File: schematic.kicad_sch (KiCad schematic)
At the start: 6 parts, among them J1 Controller, U1 ATtiny85

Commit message: pulldown
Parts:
- added R1: 100k, symbol Device:R_US
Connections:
- net Earth: now also R1.2
- net at RV1.2, U1.7 (PB2): now also R1.1
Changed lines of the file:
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@@
   (junction (at 175.26 83.82) (diameter 0) (color 0 0 0 0)
   )
-  (junction (at 149.86 115.57) (diameter 0) (color 0 0 0 0)
+  (junction (at 149.86 115.57) (diameter 0) (color 0 0 0 1)
   )
   (junction (at 166.37 115.57) (diameter 0) (color 0 0 0 1)
   )
-  (junction (at 121.92 64.77) (diameter 0) (color 194 0 0 1)
-  )
-  (junction (at 186.69 115.57) (diameter 0) (color 0 0 0 0)
-  )
-  (junction (at 166.37 64.77) (diameter 0) (color 194 0 0 1)
-  )
-  (junction (at 149.86 64.77) (diameter 0) (color 194 0 0 1)
-  )
-  (junction (at 137.16 64.77) (diameter 0) (color 194 0 0 1)
+  (junction (at 121.92 69.85) (diameter 0) (color 194 0 0 1)
+  )
+  (junction (at 186.69 115.57) (diameter 0) (color 0 0 0 1)
+  )
+  (junction (at 166.37 69.85) (diameter 0) (color 194 0 0 1)
+  )
+  (junction (at 149.86 69.85) (diameter 0) (color 194 0 0 1)
+  )
+  (junction (at 137.16 69.85) (diameter 0) (color 194 0 0 1)
+  )
+  (junction (at 139.7 115.57) (diameter 0) (color 0 0 0 1)
   )
   (junction (at 121.92 115.57) (diameter 0) (color 0 0 0 1)
   )
+  (junction (at 139.7 105.41) (diameter 0) (color 0 0 0 0)
+  )
   (junction (at 175.26 115.57) (diameter 0) (color 0 0 0 1)
   )
+  (wire (pts (xy 139.7 115.57) (xy 149.86 115.57))
+    (stroke (width 0) (type default) (color 0 0 0 1))
+  )
   (wire (pts (xy 158.75 96.52) (xy 158.75 88.9))
     (stroke (width 0) (type default))
@@
     (stroke (width 0) (type default))
   )
-  (wire (pts (xy 121.92 115.57) (xy 149.86 115.57))
-    (stroke (width 0) (type default) (color 0 0 0 1))
-  )
-  (wire (pts (xy 101.6 106.68) (xy 101.6 96.52))
+  (wire (pts (xy 121.92 115.57) (xy 139.7 115.57))
+    (stroke (width 0) (type default) (color 0 0 0 1))
+  )
+  (wire (pts (xy 101.6 105.41) (xy 101.6 96.52))
     (stroke (width 0) (type default))
   )
@@
     (stroke (width 0) (type default) (color 0 0 0 1))
   )
-  (wire (pts (xy 166.37 64.77) (xy 166.37 92.71))
-    (stroke (width 0) (type default) (color 194 0 0 1))
-  )
-  (wire (pts (xy 149.86 93.98) (xy 149.86 64.77))
+  (wire (pts (xy 166.37 69.85) (xy 166.37 92.71))
+    (stroke (width 0) (type default) (color 194 0 0 1))
+  )
+  (wire (pts (xy 149.86 93.98) (xy 149.86 69.85))
     (stroke (width 0) (type default) (color 194 0 0 1))
   )
@@
     (stroke (width 0) (type default) (color 0 0 0 1))
   )
-  (wire (pts (xy 96.52 92.71) (xy 96.52 64.77))
+  (wire (pts (xy 96.52 92.71) (xy 96.52 69.85))
     (stroke (width 0) (type default) (color 194 0 0 1))
   )
@@
   )
   (wire (pts (xy 186.69 118.11) (xy 186.69 115.57))
-    (stroke (width 0) (type default))
-  )
-  (wire (pts (xy 137.16 64.77) (xy 149.86 64.77))
+    (stroke (width 0) (type default) (color 0 0 0 1))
+  )
+  (wire (pts (xy 137.16 69.85) (xy 149.86 69.85))
     (stroke (width 0) (type default) (color 194 0 0 1))
   )
@@
     (stroke (width 0) (type default) (color 0 0 0 1))
   )
-  (wire (pts (xy 121.92 64.77) (xy 121.92 73.66))
-    (stroke (width 0) (type default) (color 194 0 0 1))
-  )
-  (wire (pts (xy 149.86 64.77) (xy 166.37 64.77))
+  (wire (pts (xy 121.92 69.85) (xy 121.92 73.66))
+    (stroke (width 0) (type default) (color 194 0 0 1))
+  )
+  (wire (pts (xy 149.86 69.85) (xy 166.37 69.85))
     (stroke (width 0) (type default) (color 194 0 0 1))
   )
@@
     (stroke (width 0) (type default) (color 0 0 0 1))
   )
-  (wire (pts (xy 186.69 81.28) (xy 186.69 64.77))
+  (wire (pts (xy 186.69 81.28) (xy 186.69 69.85))
     (stroke (width 0) (type default) (color 194 0 0 1))
   )
@@
     (stroke (width 0) (type default) (color 0 132 0 1))
   )
-  (wire (pts (xy 139.7 86.36) (xy 139.7 106.68))
+  (wire (pts (xy 139.7 86.36) (xy 139.7 105.41))
+    (stroke (width 0) (type default))
+  )
+  (wire (pts (xy 139.7 105.41) (xy 139.7 106.68))
     (stroke (width 0) (type default))
   )
@@
     (stroke (width 0) (type default) (color 0 132 0 1))
   )
-  (wire (pts (xy 139.7 106.68) (xy 101.6 106.68))
-    (stroke (width 0) (type default))
-  )
-  (wire (pts (xy 166.37 64.77) (xy 186.69 64.77))
-    (stroke (width 0) (type default) (color 194 0 0 1))
-  )
-  (wire (pts (xy 121.92 64.77) (xy 137.16 64.77))
+  (wire (pts (xy 139.7 105.41) (xy 101.6 105.41))
+    (stroke (width 0) (type default))
+  )
+  (wire (pts (xy 166.37 69.85) (xy 186.69 69.85))
+    (stroke (width 0) (type default) (color 194 0 0 1))
+  )
+  (wire (pts (xy 121.92 69.85) (xy 137.16 69.85))
     (stroke (width 0) (type default) (color 194 0 0 1))
   )
@@
     (stroke (width 0) (type default) (color 0 0 0 1))
   )
-  (wire (pts (xy 96.52 64.77) (xy 121.92 64.77))
+  (wire (pts (xy 96.52 69.85) (xy 121.92 69.85))
     (stroke (width 0) (type default) (color 194 0 0 1))
   )
@@
     (stroke (width 0) (type default))
   )
-  (wire (pts (xy 137.16 64.77) (xy 137.16 81.28))
+  (wire (pts (xy 137.16 69.85) (xy 137.16 81.28))
     (stroke (width 0) (type default) (color 194 0 0 1))
   )
@@
     (stroke (width 0) (type default) (color 0 0 0 1))
   )
+  (wire (pts (xy 139.7 114.3) (xy 139.7 115.57))
+    (stroke (width 0) (type default) (color 0 0 0 1))
+  )
   (wire (pts (xy 101.6 96.52) (xy 100.33 96.52))
-    (stroke (width 0) (type default))
-  )
-  (wire (pts (xy 186.69 115.57) (xy 181.61 115.57))
     (stroke (width 0) (type default))
   )
@@
         )
       )
+    )
+  )
+  (symbol (lib_id "Device:R_US") (at 139.7 110.49 0) (unit 1)
+    (in_bom yes) (on_board yes) (dnp no) (fields_autoplaced)
+    (property "Reference" "R1" (at 142.24 109.22 0)
+      (effects (font (size 1.27 1.27)) (justify left))
+    )
+    (property "Value" "100k" (at 142.24 111.76 0)
+      (effects (font (size 1.27 1.27)) (justify left))
+    )
+    (property "Footprint" "" (at 140.716 110.744 90)
+      (effects (font (size 1.27 1.27)) hide)
+    )
+    (property "Datasheet" "~" (at 139.7 110.49 0)
+      (effects (font (size 1.27 1.27)) hide)
+    )
+    (pin "2")
+    (pin "1")
+    (instances
+      (project "schematic"
+        (path "/525ec903-8040-4be3-a233-c9b42088bb47"
+          (reference "R1") (unit 1)
+        )
+      )

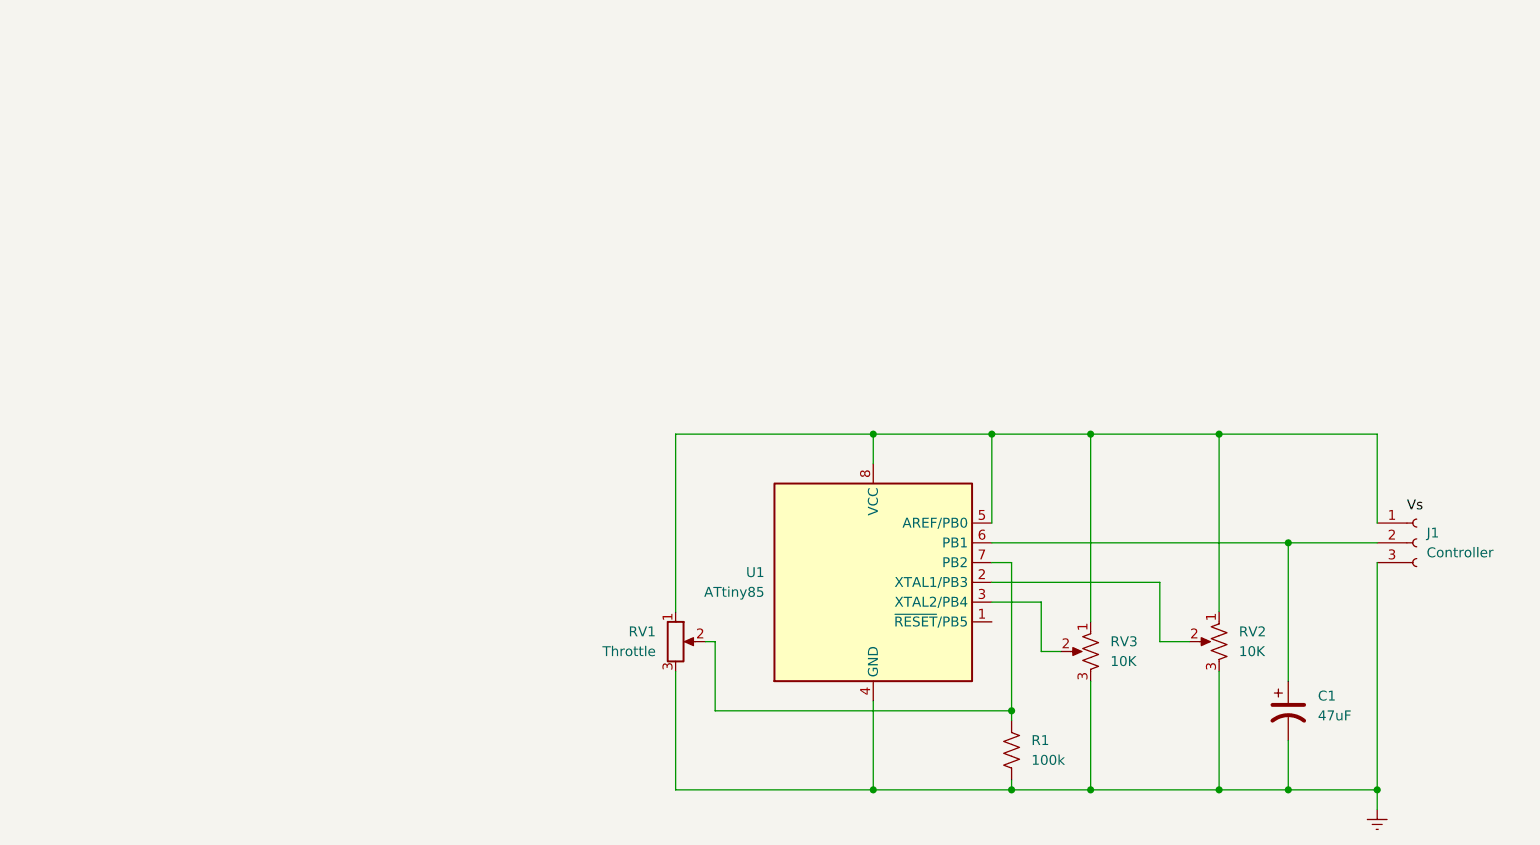
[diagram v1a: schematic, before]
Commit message: add filter resistor
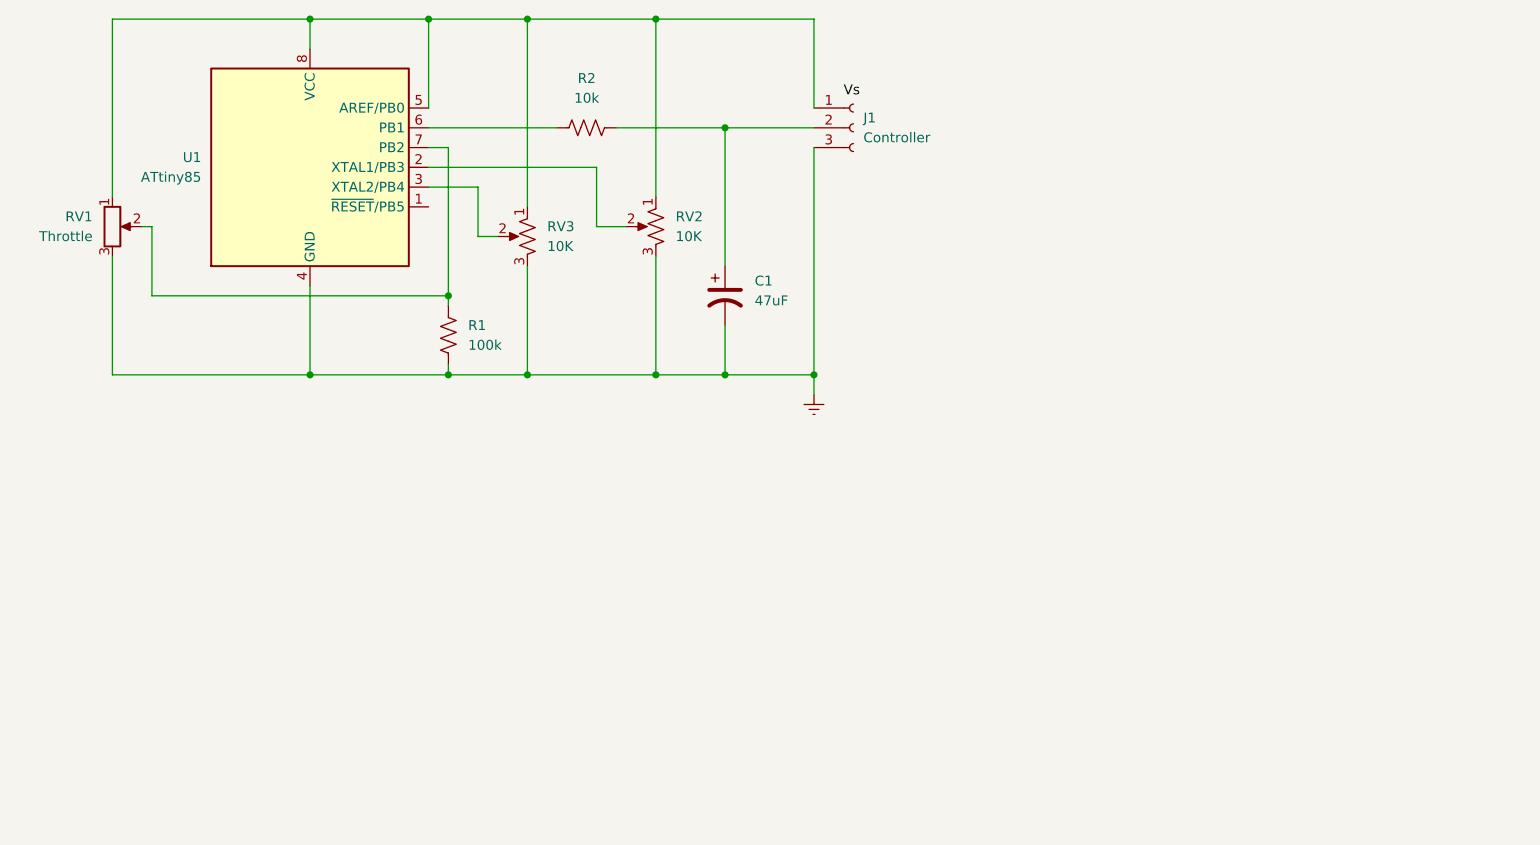
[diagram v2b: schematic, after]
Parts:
- added R2: 10k, symbol Device:R_US
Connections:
- net at C1.1, J1.2 (Pin_2): now also R2.1; no longer U1.6 (PB1)
- new net: R2.2, U1.6 (PB1)
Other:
- title: (none) -> bike-aid-throtle
- moved on the sheet: C1, J1, R1, RV1, RV2, RV3, U1
